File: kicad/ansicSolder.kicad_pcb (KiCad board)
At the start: 2 copper layers, 100 x 97 mm, 62 parts, among them J1 AudioJack4, J2 AudioJack4, J3 Conn_01x02_Socket, SW1 SW_Push, SW10 SW_Push, SW11 SW_Push, SW12 SW_Push, SW13 SW_Push, SW14 SW_Push, SW15 SW_Push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

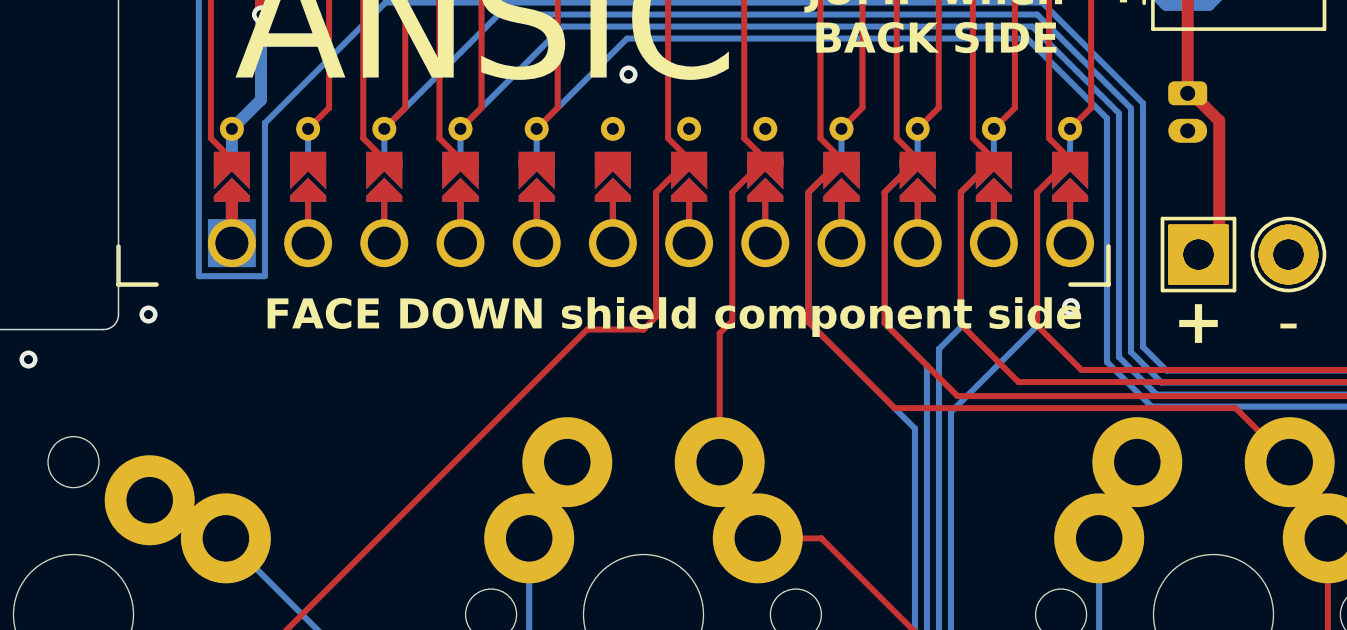
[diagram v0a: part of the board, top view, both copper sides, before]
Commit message: fix confusing legend of silkscreen
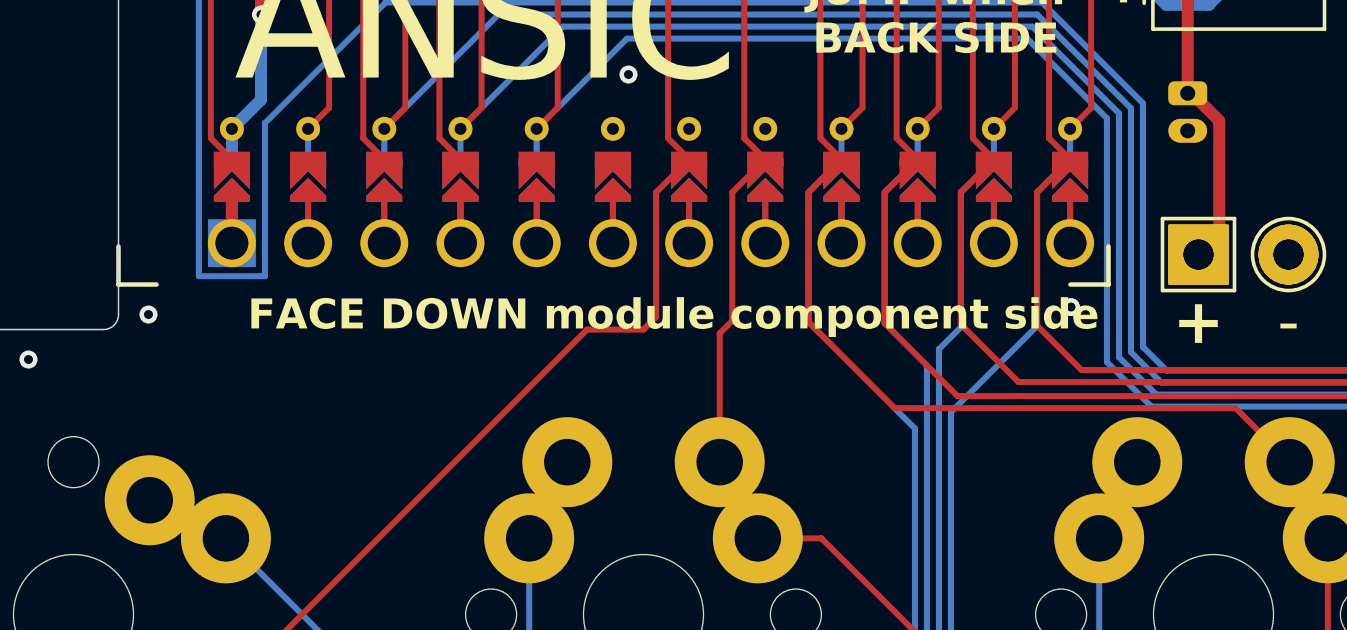
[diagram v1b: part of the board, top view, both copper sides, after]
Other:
- board text added: "FACE DOWN module component side"
- board text removed: "FACE DOWN shield component side"
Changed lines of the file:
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@@
 		(layer "Edge.Cuts")
 	)
-	(gr_text "FACE DOWN shield component side"
+	(gr_text "FACE DOWN module component side"
 		(at 92.5 48 0)
 		(layer "F.SilkS")
@@
 		)
 	)
-	(gr_text "FACE DOWN shield component side"
+	(gr_text "FACE DOWN module component side"
 		(at 92.5 48 -0)
 		(layer "B.SilkS")
